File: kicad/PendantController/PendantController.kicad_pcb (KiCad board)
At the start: 2 copper layers, 55 x 95 mm, 27 parts, among them J1 RotaryEncoder, J10 Btn7, J11 Btn8, J2 Switches, J3 DC24V, J4 Btn1, J5 Btn2, J6 Btn3, J7 Btn4, J8 Btn5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

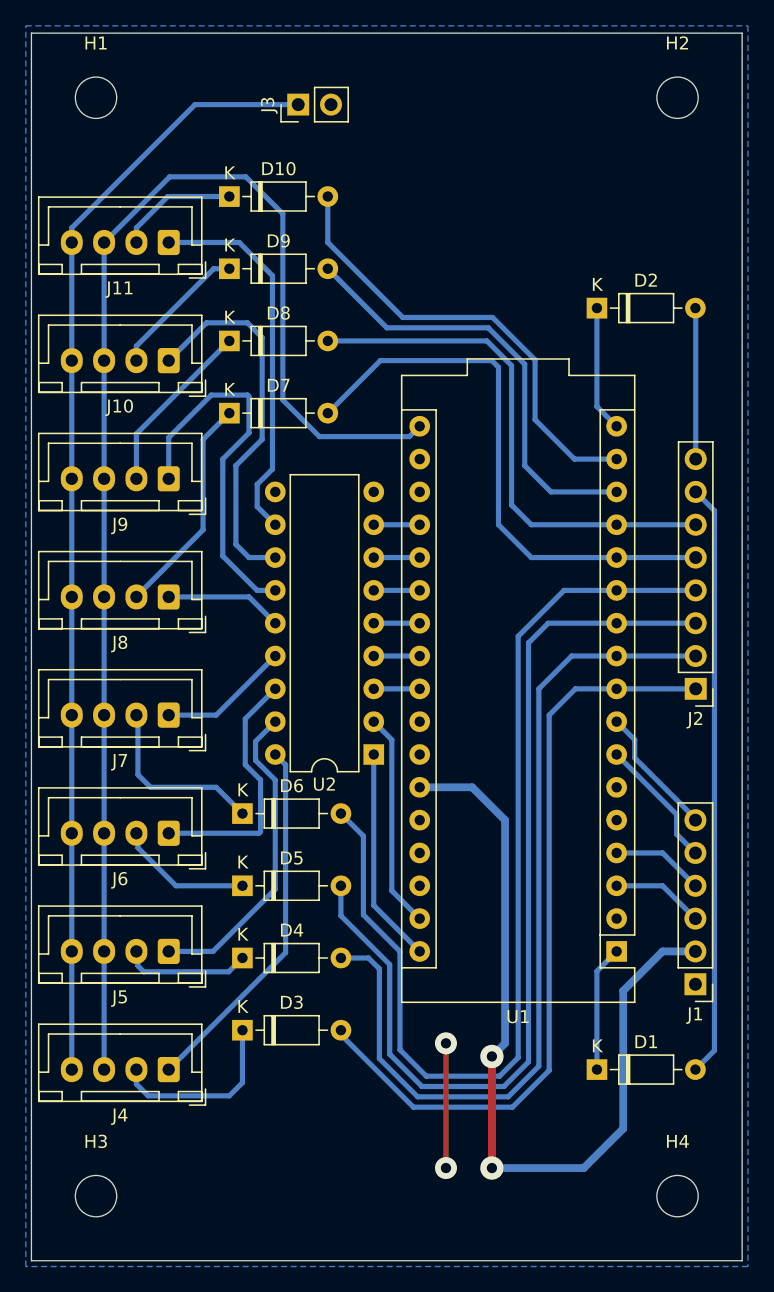
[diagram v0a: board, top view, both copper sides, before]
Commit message: Added cable plug adapter, use 0.4mm spacing for PCB
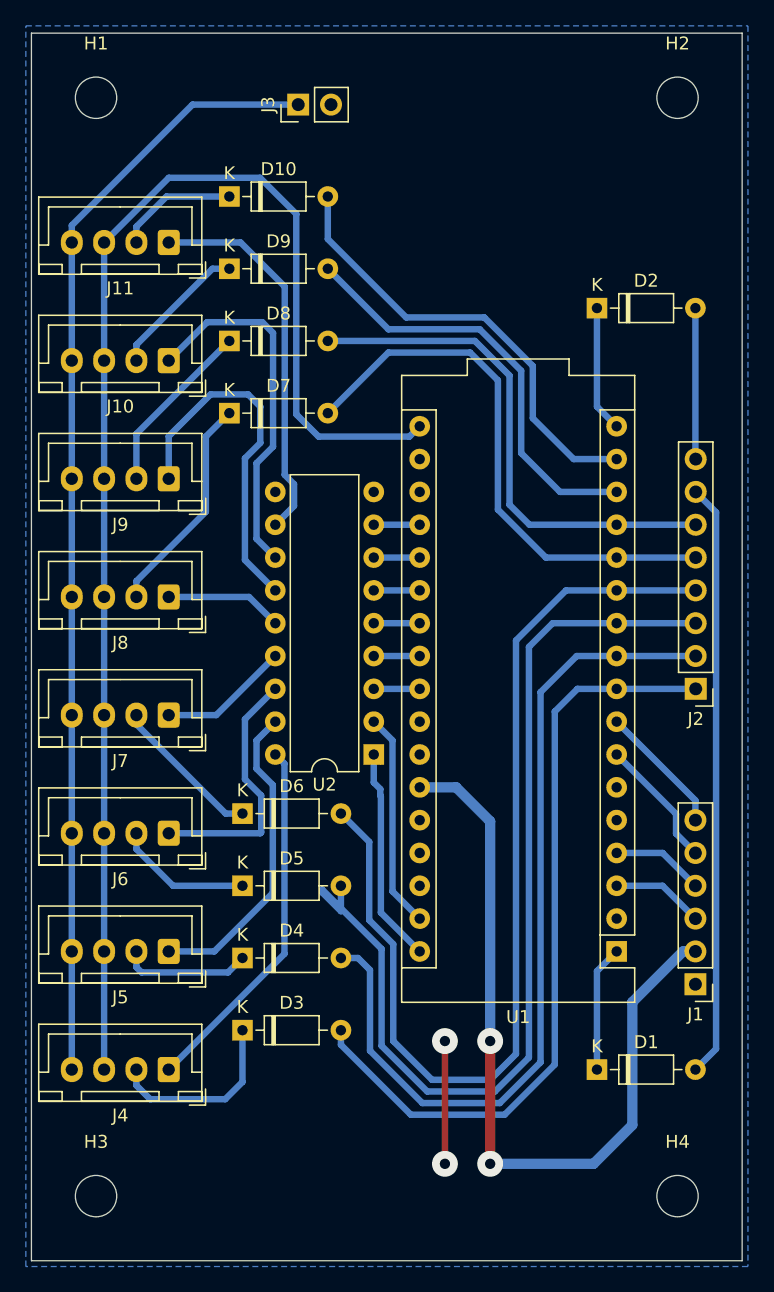
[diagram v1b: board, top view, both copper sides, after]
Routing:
- net /In3: track 73.2 -> 77.6 mm
- net +5V: track 63.9 -> 61.3 mm
- net Net-(D6-K): track 13.9 -> 11.8 mm
- net Net-(J9-Pin_1): track 29.2 -> 27.8 mm
- net Net-(J10-Pin_1): track 29.2 -> 28.2 mm
- net /In7: track 34.1 -> 33.2 mm
- net /In1: track 59.6 -> 60.5 mm
- net /LED1: track 16.7 -> 17.5 mm
- net /In5: track 43.6 -> 42.8 mm

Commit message: Updated PCB layout
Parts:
- added R1: 10, Resistor_THT:R_Axial_DIN0309_L9.0mm_D3.2mm_P12.70mm_Horizontal, F.Cu at (119.3, 65.5)
- moved D8 28.2 mm to (115.9, 112.0)
- moved D7 28.1 mm to (115.9, 117.5)
- moved D2 17.6 mm to (136.0, 65.5)
- moved J1 12.1 mm to (151.3, 121.5)
- moved D1 12.1 mm to (143.7, 128.1)
- moved J2 12.1 mm to (151.4, 98.6)
- moved U1 12.1 mm to (145.2, 119.0)
- moved U2 12.1 mm to (126.0, 103.8)
- moved J3 8.14 mm to (112.5, 65.5)
- moved D5 2.86 mm to (116.0, 128.8)
- moved D3 2.86 mm to (116.0, 140.0)
- moved D4 2.86 mm to (116.0, 134.4)
- moved D6 2.86 mm to (116.0, 123.2)
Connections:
- J3 pad 2: GND -> Net-(J3-Pin_2)
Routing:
- net /In6: track 40.2 -> 80.8 mm
- net /In5: track 42.8 -> 75.7 mm
- net Net-(J8-Pin_1): track 9.09 -> 37.1 mm
- net Net-(J7-Pin_1): track 10.1 -> 36.4 mm
- net Net-(J10-Pin_1): track 28.2 -> 9.08 mm
- net Net-(J9-Pin_1): track 27.8 -> 9.17 mm
- net Net-(J6-Pin_1): track 19.8 -> 36.9 mm
- net Net-(J4-Pin_1): track 28.4 -> 43.3 mm
- net Net-(J5-Pin_1): track 24.3 -> 39.1 mm
- net /In3: track 77.6 -> 63.8 mm
- net Net-(J11-Pin_1): track 29.7 -> 17.9 mm
- net /BtnOut: track 108.4 -> 98.1 mm
- net /In4: track 78.4 -> 68.7 mm
- net /In8: track 35.1 -> 25.7 mm
- net +24V: track 86.9 -> 78.7 mm
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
